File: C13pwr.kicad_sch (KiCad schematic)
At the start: 16 parts, among them IC2 MPM3610AGQV-P, U16 INA181-A4, U2 MIC5235-3.3, U4 78M05

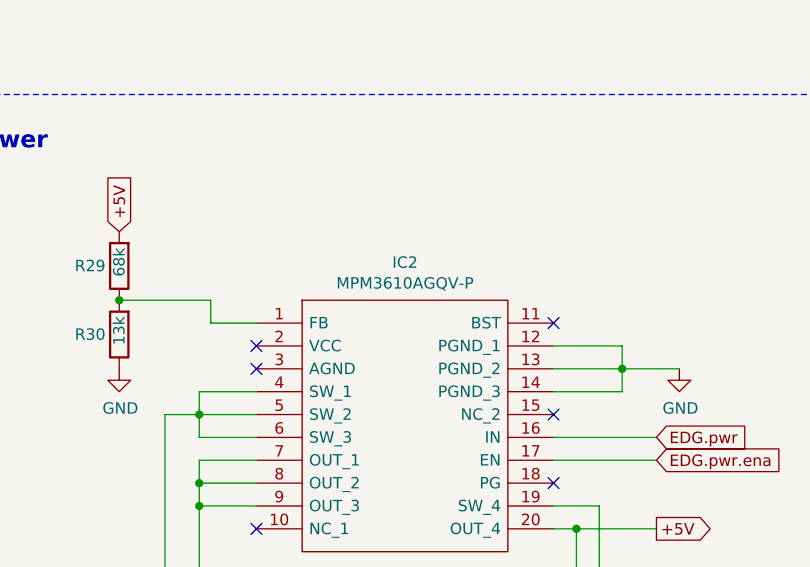
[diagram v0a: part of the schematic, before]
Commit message: mod: conversion to KiCad 9
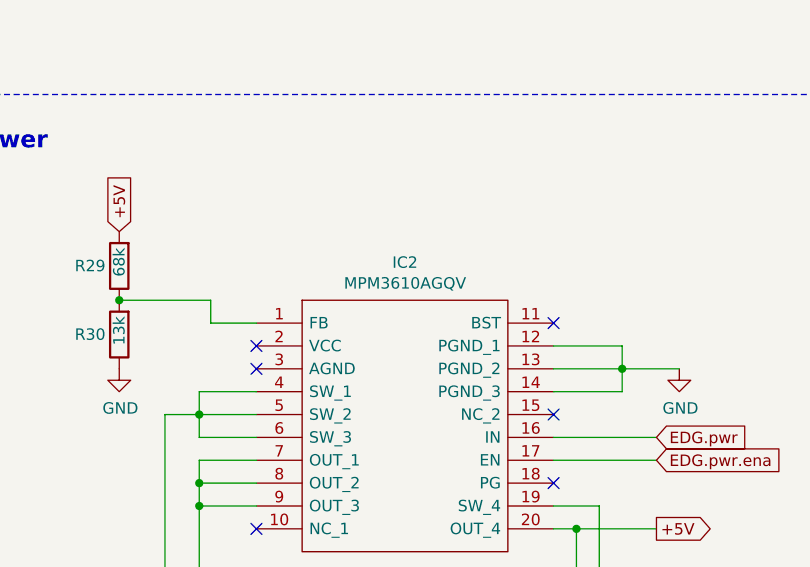
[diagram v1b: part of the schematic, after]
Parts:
- IC2: value MPM3610AGQV-P -> MPM3610AGQV; LCSC Part # C6097430 -> C5173872
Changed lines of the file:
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@@
 	(title_block
 		(title "RTB C13 Module")
-		(date "2023-10-25")
-		(rev "1")
+		(date "2025-10-14")
+		(rev "2")
 		(company "Frank Schumacher")
 		(comment 1 "Track Sensor")
@@
 			)
 		)
-		(property "Value" "MPM3610AGQV-P"
+		(property "Value" "MPM3610AGQV"
 			(at 215.9 43.8404 0)
 			(effects
@@
 			)
 		)
-		(property "LCSC Part #" "C6097430"
+		(property "LCSC Part #" "C5173872"
 			(at 199.39 48.26 0)
 			(effects
